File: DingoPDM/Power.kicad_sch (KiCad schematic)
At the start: 31 parts, among them J6 SHORT, SW2 AlwaysOn, U13 VXO780x-500-M, U14 TLP2366(V4-TPL,E, U15 LD1117S33CTR, U16 ISP752R

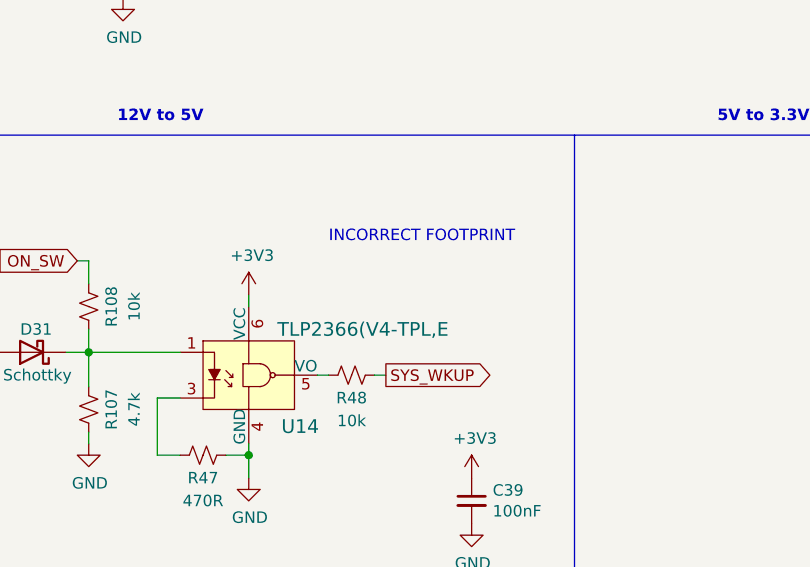
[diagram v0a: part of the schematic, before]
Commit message: Wrong opto-isolator part number
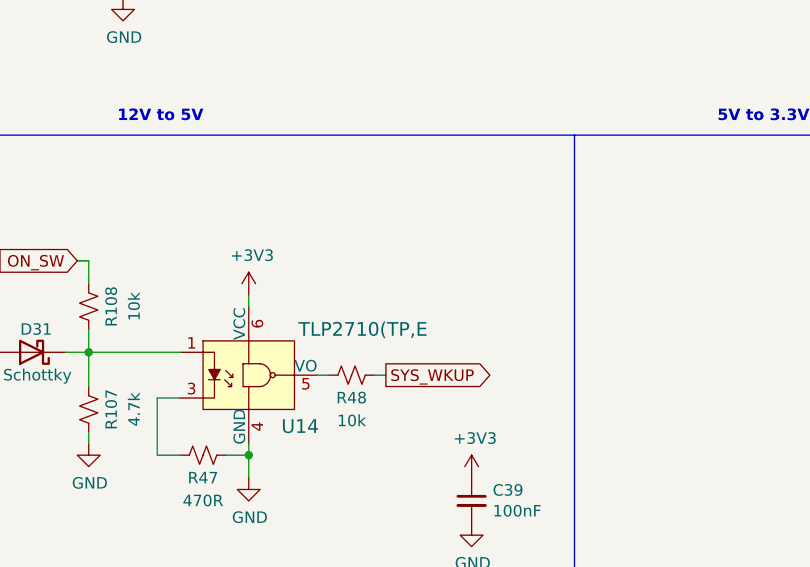
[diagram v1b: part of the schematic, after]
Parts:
- U14: value TLP2366(V4-TPL,E -> TLP2710(TP,E; Digi-Key_PN TLP2366(V4-TPLECT-ND -> TLP2710(TPECT-ND
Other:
- note removed: "INCORRECT FOOTPRINT"

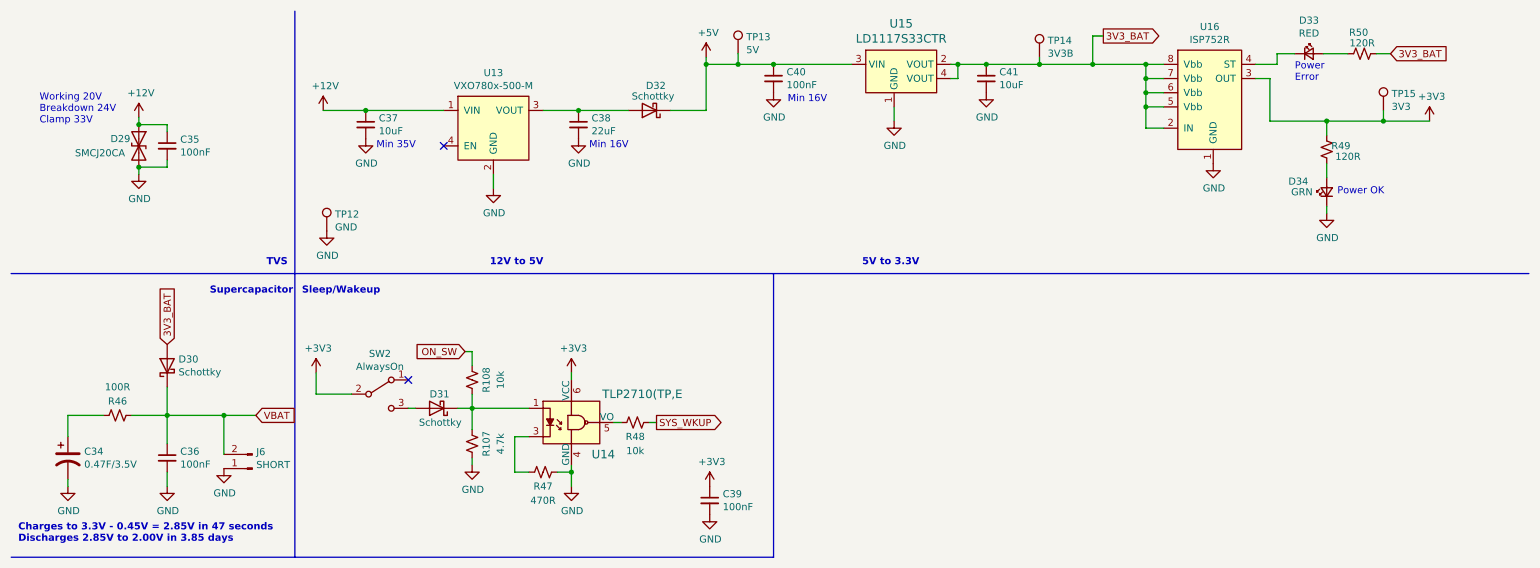
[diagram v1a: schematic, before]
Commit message: Changed schematic sheet size to letter
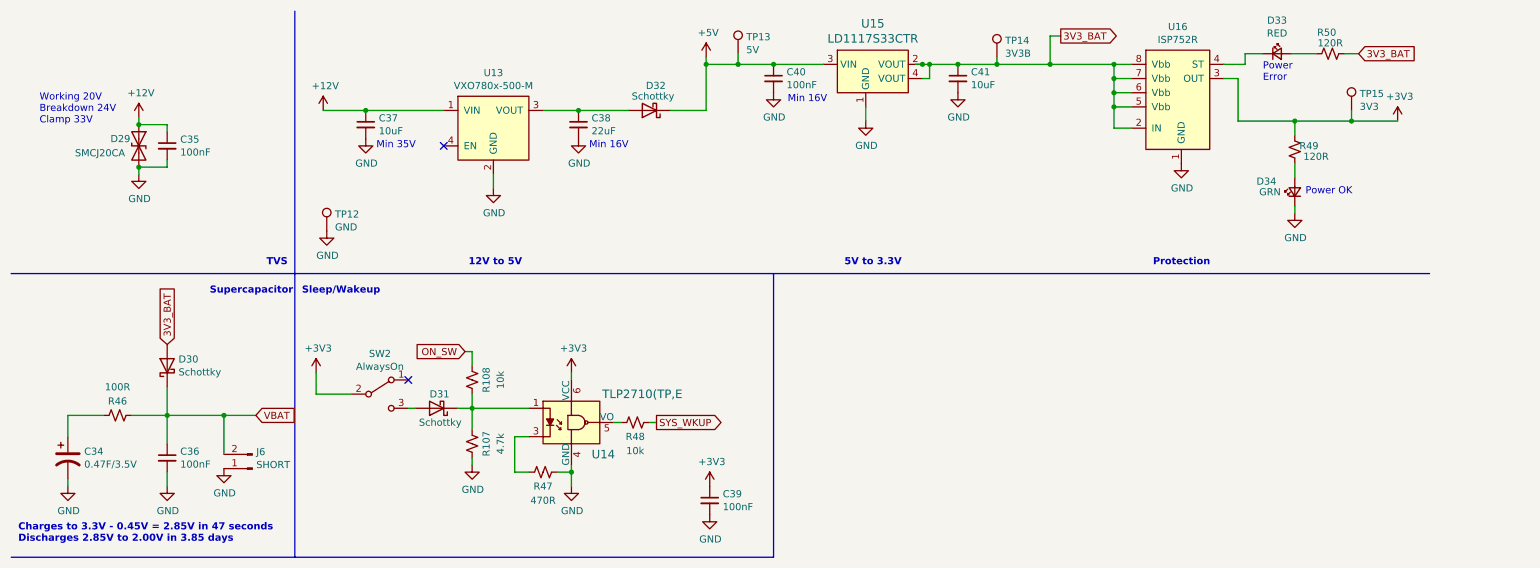
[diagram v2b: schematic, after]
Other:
- note added: "Protection"
- moved on the sheet: C41, D33, D34, R49, R50, TP14, TP15, U15, U16
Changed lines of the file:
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@@
 (kicad_sch (version 20230121) (generator eeschema)
-  (paper "A4")
+  (paper "USLetter")
   (title_block
     (title "Dingo_PDM")
-    (date "2023-02-23")
+    (date "2023-04-01")
     (rev "v5")
     (comment 3 "github.com/corygrant")

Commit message: Redesigned to a smaller unit
4x high current, 2x med current, 4x low current, 2x digital inputs
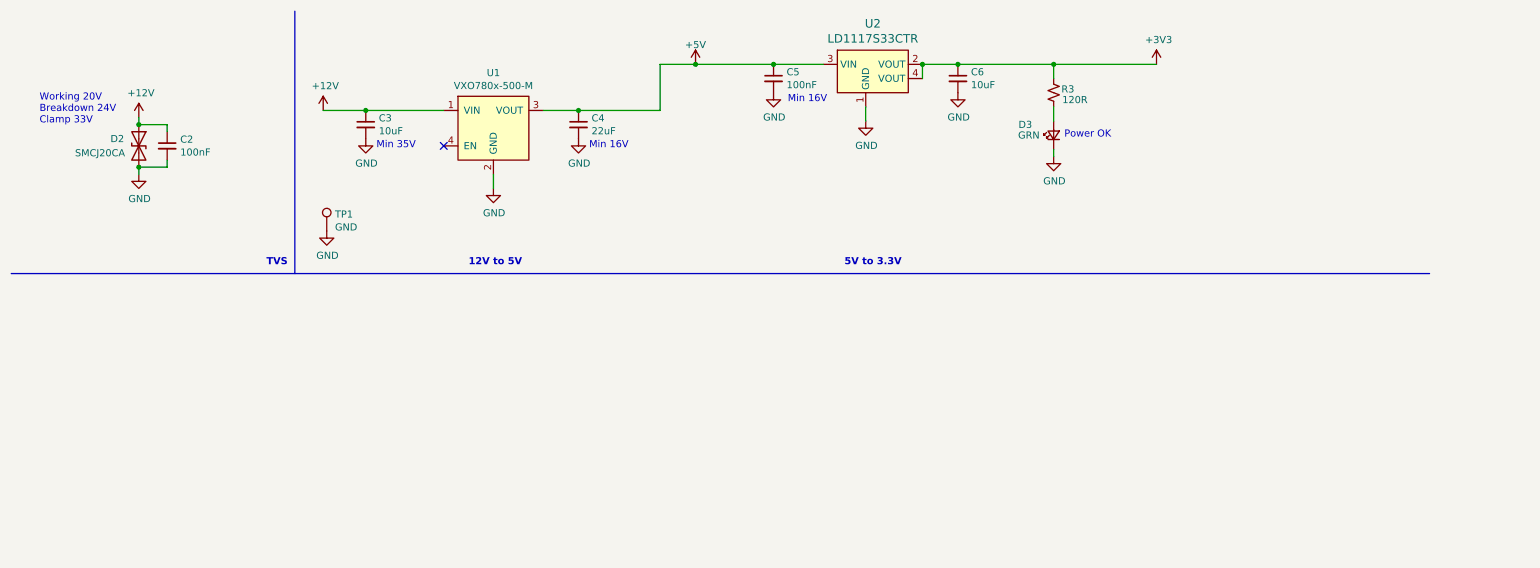
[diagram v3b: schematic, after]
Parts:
- removed C34: 0.47F/3.5V, SuperCap:FC0V474ZFTBR24, symbol Device:CP1
- removed C36, C39: 100nF, Capacitor_SMD:C_0805_2012Metric, symbol Device:C_Small
- removed D30, D31, D32: Schottky, Diode_SMD:D_SOD-123, symbol Device:D_Schottky
- removed D33: RED, LED_SMD:LED_0805_2012Metric, symbol Device:LED_Small
- removed J6: SHORT, Jumper:SolderJumper-2_P1.3mm_Open_Pad1.0x1.5mm, symbol Connector:Conn_01x02_Male
- removed R107: 4.7k, Resistor_SMD:R_0805_2012Metric, symbol Device:R_Small_US
- removed R108, R48: 10k, Resistor_SMD:R_0805_2012Metric, symbol Device:R_Small_US
- removed R46: 100R, Resistor_SMD:R_0805_2012Metric, symbol Device:R_Small_US
- removed R47: 470R, Resistor_SMD:R_0805_2012Metric, symbol Device:R_Small_US
- removed R50: 120R, Resistor_SMD:R_0805_2012Metric, symbol Device:R_Small_US
- removed SW2: AlwaysOn, SlideSwitch:CJS-1200TB, symbol Switch:SW_SPDT
- removed TP13: 5V, TestPoint:TestPoint_Pad_D1.0mm, symbol Connector:TestPoint
- removed TP14: 3V3B, TestPoint:TestPoint_Pad_D1.0mm, symbol Connector:TestPoint
- removed TP15: 3V3, TestPoint:TestPoint_Pad_D1.0mm, symbol Connector:TestPoint
- removed U14: TLP2710(TP,E, Profet:TLP2710(TP,E, symbol dk_Optoisolators-Logic-Output:TLP2361_TPL_E
- removed U16: ISP752R, Profet:PG-DSO-8, symbol Profet:ISP752R
- C2: renamed from C35; LCSC (none) -> C49678
- C3: renamed from C37; LCSC (none) -> C15850
- C4: renamed from C38; LCSC (none) -> C45783
- C5: renamed from C40; LCSC (none) -> C49678
- C6: renamed from C41; LCSC (none) -> C15850
- D2: renamed from D29; LCSC (none) -> C2760132
- D3: renamed from D34; LCSC (none) -> C2899888
- U2: renamed from U15; LCSC (none) -> C35879
- renumbered R49 to R3, TP12 to TP1, U13 to U1
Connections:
- net 3V3_BAT is gone; now on net +3V3: C6.1, U2.2 (VOUT), U2.4 (VOUT)
- net +5V: now also C4.1, U1.3 (VOUT)
- no-connect marks 2 -> 1
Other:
- note removed: "Charges to 3.3V - 0.45V = 2.85V in 47 seconds Discharges 2.85V to 2.00V in 3.85 days"
- note removed: "Power Error"
- note removed: "Protection"
- note removed: "Sleep/Wakeup"
- note removed: "Supercapacitor"
- moved on the sheet: D3, R3

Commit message: Added documentation, finished and cleaned design
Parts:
- R3: Digi-Key_PN 311-100CRCT-ND -> 311-120CRCT-ND; LCSC (none) -> C229076
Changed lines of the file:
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@@
   (title_block
     (title "Dingo_PDM")
-    (date "2023-04-01")
-    (rev "v5")
+    (date "2023-07-28")
+    (rev "v6")
     (comment 3 "github.com/corygrant")
     (comment 4 "Cory Grant")
@@
       (effects (font (size 1.27 1.27)) hide)
     )
-    (property "Digi-Key_PN" "311-100CRCT-ND" (at 199.39 28.575 0)
-      (effects (font (size 1.27 1.27)) hide)
-    )
-    (property "LCSC" "" (at 199.39 28.575 0)
-      (effects (font (size 1.27 1.27)) hide)
-    )
+    (property "Digi-Key_PN" "311-120CRCT-ND" (at 199.39 28.575 0)
+      (effects (font (size 1.27 1.27)) hide)
+    )
+    (property "LCSC" "C229076" (at 199.39 28.575 0)
+      (effects (font (size 1.27 1.27)) hide)
+    )

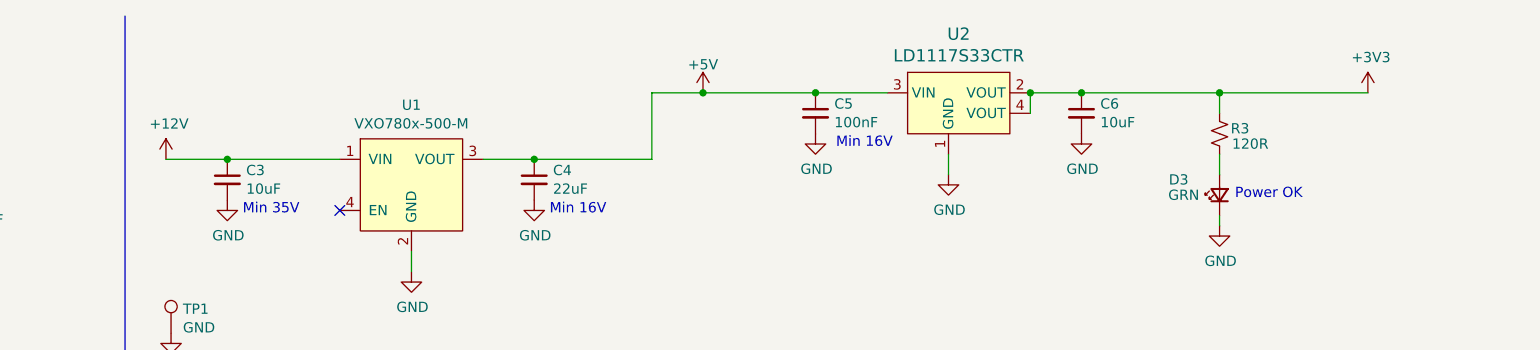
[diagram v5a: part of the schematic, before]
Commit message: Add diode, disconnect PB13, fix USB VBUS
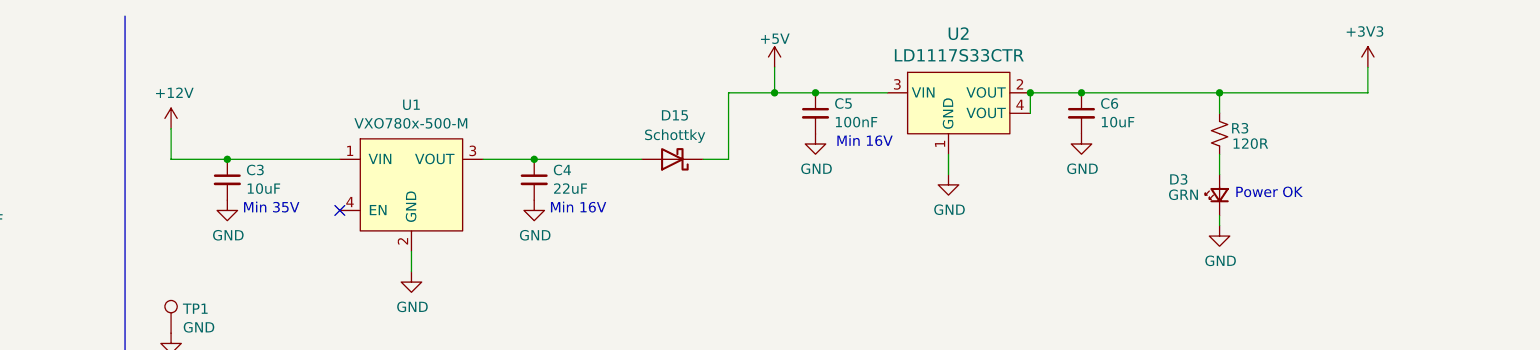
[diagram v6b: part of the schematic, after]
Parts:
- added D15: Schottky, Diode_SMD:D_SOD-123, symbol Device:D_Schottky
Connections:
- net +5V: now also D15.1 (K); no longer C4.1, U1.3 (VOUT)
- new net: C4.1, D15.2 (A), U1.3 (VOUT)
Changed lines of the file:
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@@
   (title_block
     (title "Dingo_PDM")
-    (date "2023-09-04")
-    (rev "v7.1")
+    (date "2023-09-11")
+    (rev "v7.2")
     (comment 3 "github.com/corygrant")
     (comment 4 "Cory Grant")
@@
   (junction (at 199.39 23.495) (diameter 0) (color 0 0 0 0)
   )
-  (junction (at 135.255 23.495) (diameter 0) (color 0 0 0 0)
+  (junction (at 144.145 23.495) (diameter 0) (color 0 0 0 0)
   )
   (junction (at 114.3 31.75) (diameter 0) (color 0 0 0 0)
@@
   )
   (no_connect (at 90.17 38.1))
+  (wire (pts (xy 217.805 20.32) (xy 217.805 23.495))
+    (stroke (width 0) (type default))
+  )
   (wire (pts (xy 35.56 41.91) (xy 40.64 41.91))
     (stroke (width 0) (type default))
@@
     (stroke (width 0) (type default))
   )
-  (wire (pts (xy 128.905 31.75) (xy 128.905 23.495))
+  (wire (pts (xy 135.255 31.75) (xy 138.43 31.75))
+    (stroke (width 0) (type default))
+  )
+  (wire (pts (xy 138.43 31.75) (xy 138.43 23.495))
     (stroke (width 0) (type default))
   )
@@
     (stroke (width 0) (type default))
   )
-  (wire (pts (xy 114.3 31.75) (xy 128.905 31.75))
+  (wire (pts (xy 144.145 23.495) (xy 149.225 23.495))
+    (stroke (width 0) (type default))
+  )
+  (wire (pts (xy 114.3 31.75) (xy 127.635 31.75))
     (stroke (width 0) (type default))
   )
@@
     (stroke (width 0) (type default))
   )
+  (wire (pts (xy 69.215 27.94) (xy 69.215 31.75))
+    (stroke (width 0) (type default))
+  )
   (wire (pts (xy 175.895 23.495) (xy 182.245 23.495))
     (stroke (width 0) (type default))
@@
     (stroke (width 0) (type default))
   )
-  (wire (pts (xy 68.58 31.75) (xy 76.2 31.75))
+  (wire (pts (xy 69.215 31.75) (xy 76.2 31.75))
     (stroke (width 0) (type default))
   )
@@
     (stroke (width 0) (type default))
   )
-  (wire (pts (xy 135.255 23.495) (xy 149.225 23.495))
-    (stroke (width 0) (type default))
-  )
-  (wire (pts (xy 128.905 23.495) (xy 135.255 23.495))
+  (wire (pts (xy 138.43 23.495) (xy 144.145 23.495))
     (stroke (width 0) (type default))
   )
@@
   )
   (wire (pts (xy 35.56 33.02) (xy 35.56 34.29))
+    (stroke (width 0) (type default))
+  )
+  (wire (pts (xy 144.145 20.32) (xy 144.145 23.495))
     (stroke (width 0) (type default))
   )
@@
     (effects (font (size 1.27 1.27)) (justify left bottom))
   )
-  (symbol (lib_id "power:+12V") (at 68.58 31.75 0) (unit 1)
-    (in_bom yes) (on_board yes) (dnp no)
-    (property "Reference" "#PWR07" (at 68.58 35.56 0)
-      (effects (font (size 1.27 1.27)) hide)
-    )
-    (property "Value" "+12V" (at 68.961 27.3558 0)
-      (effects (font (size 1.27 1.27)))
-    )
-    (property "Footprint" "" (at 68.58 31.75 0)
-      (effects (font (size 1.27 1.27)) hide)
-    )
-    (property "Datasheet" "" (at 68.58 31.75 0)
+  (symbol (lib_id "power:+12V") (at 69.215 27.94 0) (unit 1)
+    (in_bom yes) (on_board yes) (dnp no)
+    (property "Reference" "#PWR07" (at 69.215 31.75 0)
+      (effects (font (size 1.27 1.27)) hide)
+    )
+    (property "Value" "+12V" (at 69.596 23.5458 0)
+      (effects (font (size 1.27 1.27)))
+    )
+    (property "Footprint" "" (at 69.215 27.94 0)
+      (effects (font (size 1.27 1.27)) hide)
+    )
+    (property "Datasheet" "" (at 69.215 27.94 0)
       (effects (font (size 1.27 1.27)) hide)
     )
@@
     )
   )
-  (symbol (lib_id "power:+3V3") (at 217.805 23.495 0) (unit 1)
-    (in_bom yes) (on_board yes) (dnp no)
-    (property "Reference" "#PWR017" (at 217.805 27.305 0)
-      (effects (font (size 1.27 1.27)) hide)
-    )
-    (property "Value" "+3V3" (at 218.186 19.1008 0)
-      (effects (font (size 1.27 1.27)))
-    )
-    (property "Footprint" "" (at 217.805 23.495 0)
-      (effects (font (size 1.27 1.27)) hide)
-    )
-    (property "Datasheet" "" (at 217.805 23.495 0)
+  (symbol (lib_id "power:+3V3") (at 217.805 20.32 0) (mirror y) (unit 1)
+    (in_bom yes) (on_board yes) (dnp no)
+    (property "Reference" "#PWR017" (at 217.805 24.13 0)
+      (effects (font (size 1.27 1.27)) hide)
+    )
+    (property "Value" "+3V3" (at 217.424 15.9258 0)
+      (effects (font (size 1.27 1.27)))
+    )
+    (property "Footprint" "" (at 217.805 20.32 0)
+      (effects (font (size 1.27 1.27)) hide)
+    )
+    (property "Datasheet" "" (at 217.805 20.32 0)
       (effects (font (size 1.27 1.27)) hide)
     )
@@
     )
   )
-  (symbol (lib_id "power:+5V") (at 135.255 23.495 0) (unit 1)
+  (symbol (lib_id "Device:D_Schottky") (at 131.445 31.75 180) (unit 1)
     (in_bom yes) (on_board yes) (dnp no) (fields_autoplaced)
-    (property "Reference" "#PWR012" (at 135.255 27.305 0)
-      (effects (font (size 1.27 1.27)) hide)
-    )
-    (property "Value" "+5V" (at 135.255 19.9931 0)
-      (effects (font (size 1.27 1.27)))
-    )
-    (property "Footprint" "" (at 135.255 23.495 0)
-      (effects (font (size 1.27 1.27)) hide)
-    )
-    (property "Datasheet" "" (at 135.255 23.495 0)
-      (effects (font (size 1.27 1.27)) hide)
-    )
+    (property "Reference" "D15" (at 131.7625 26.3357 0)
+      (effects (font (size 1.27 1.27)))
+    )
+    (property "Value" "Schottky" (at 131.7625 28.7599 0)
+      (effects (font (size 1.27 1.27)))
+    )
+    (property "Footprint" "Diode_SMD:D_SOD-123" (at 131.445 31.75 0)
+      (effects (font (size 1.27 1.27)) hide)
+    )
+    (property "Datasheet" "" (at 131.445 31.75 0)
+      (effects (font (size 1.27 1.27)) hide)
+    )
+    (property "Digi-Key_PN" "1727-2394-1-ND" (at 131.445 31.75 0)
+      (effects (font (size 1.27 1.27)) hide)
+    )
+    (property "LCSC" "C179426" (at 131.445 31.75 0)
+      (effects (font (size 1.27 1.27)) hide)
+    )
+    (pin "1")
+    (pin "2")
+    (instances
+      (project "DingoPDM"
+        (path "/8948e307-9174-4227-9c28-3ff885e6e83d/00000000-0000-0000-0000-00005f5b308f"
+          (reference "D15") (unit 1)
+        )
+        (path "/8948e307-9174-4227-9c28-3ff885e6e83d/00000000-0000-0000-0000-00005f5cf2eb"
+          (reference "D18") (unit 1)
+        )
+      )
+    )
+  )
+  (symbol (lib_id "power:+5V") (at 144.145 20.32 0) (unit 1)
+    (in_bom yes) (on_board yes) (dnp no) (fields_autoplaced)
+    (property "Reference" "#PWR012" (at 144.145 24.13 0)
+      (effects (font (size 1.27 1.27)) hide)
+    )
+    (property "Value" "+5V" (at 144.145 16.8181 0)
+      (effects (font (size 1.27 1.27)))
+    )
+    (property "Footprint" "" (at 144.145 20.32 0)
+      (effects (font (size 1.27 1.27)) hide)
+    )
+    (property "Datasheet" "" (at 144.145 20.32 0)
+      (effects (font (size 1.27 1.27)) hide)
+    )
